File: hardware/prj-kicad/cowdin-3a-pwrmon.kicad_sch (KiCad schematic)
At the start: 2 parts, among them P1 CONN_9, P2 CONN_9

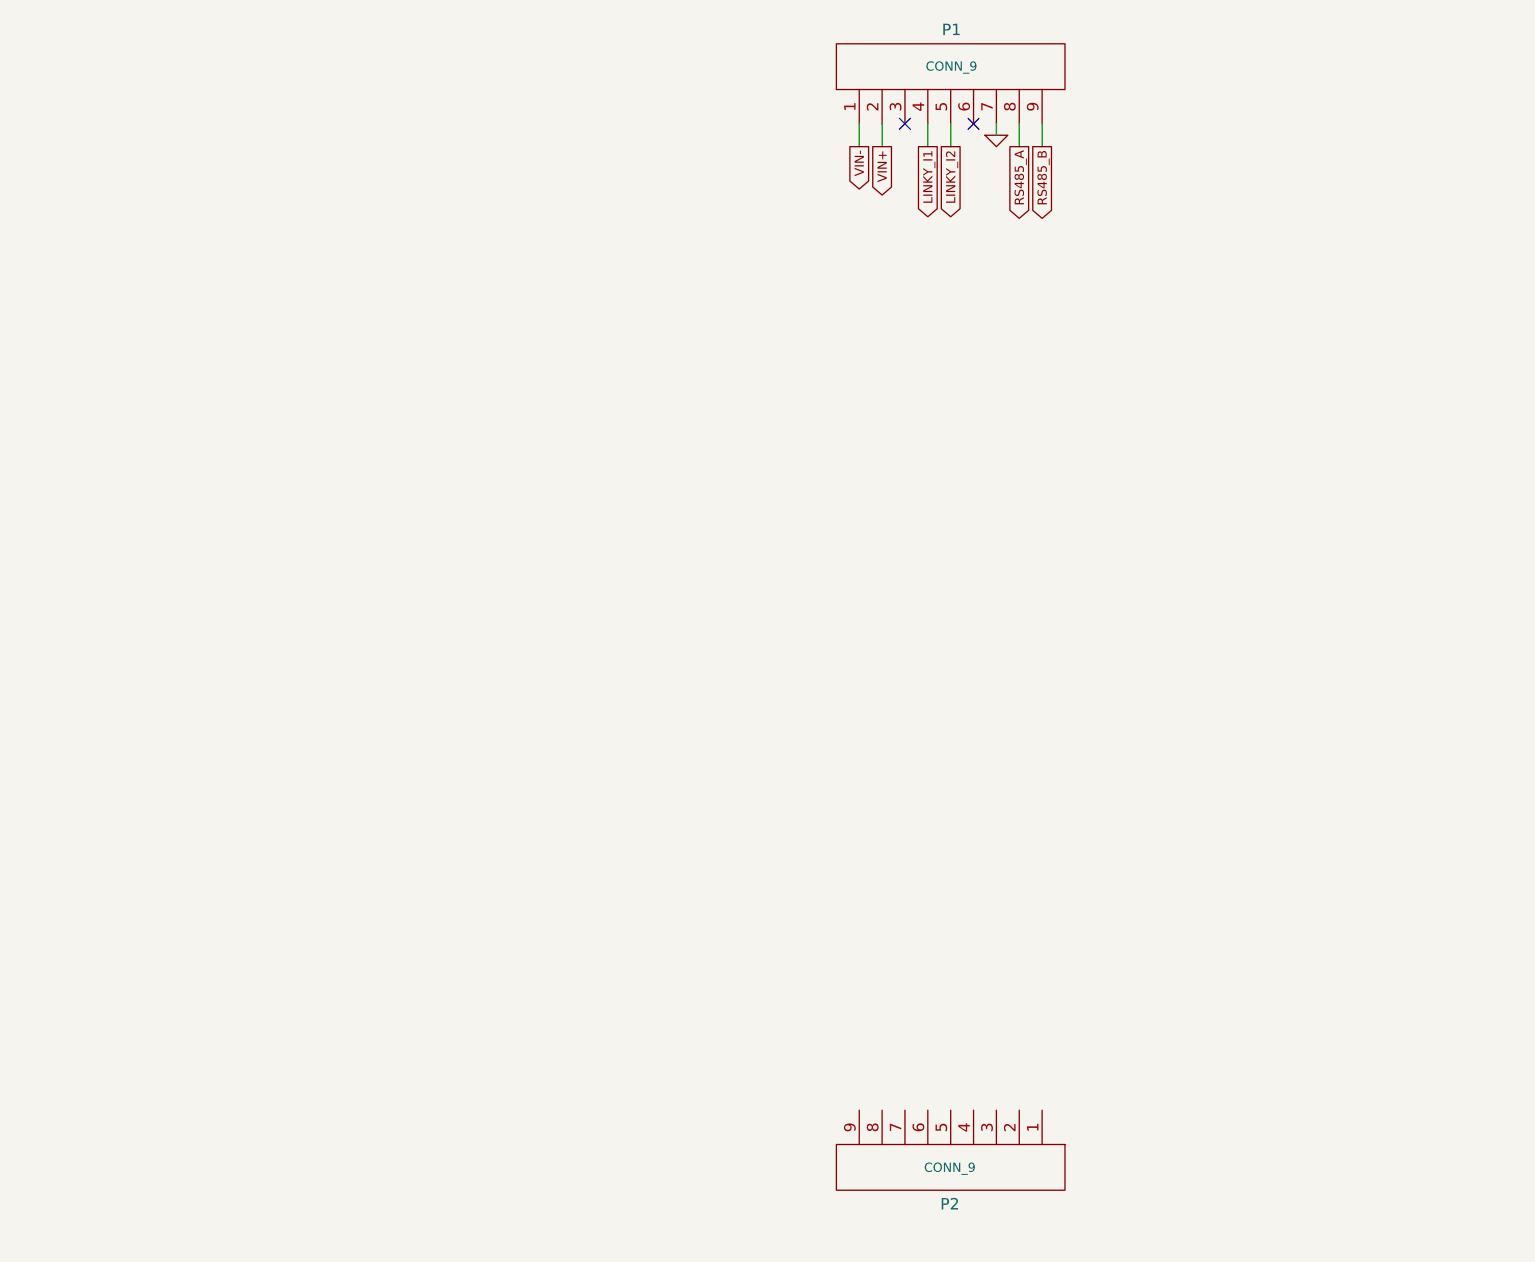
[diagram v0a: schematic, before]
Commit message: Hardware: Add communication interfaces (RS485 and Linky)
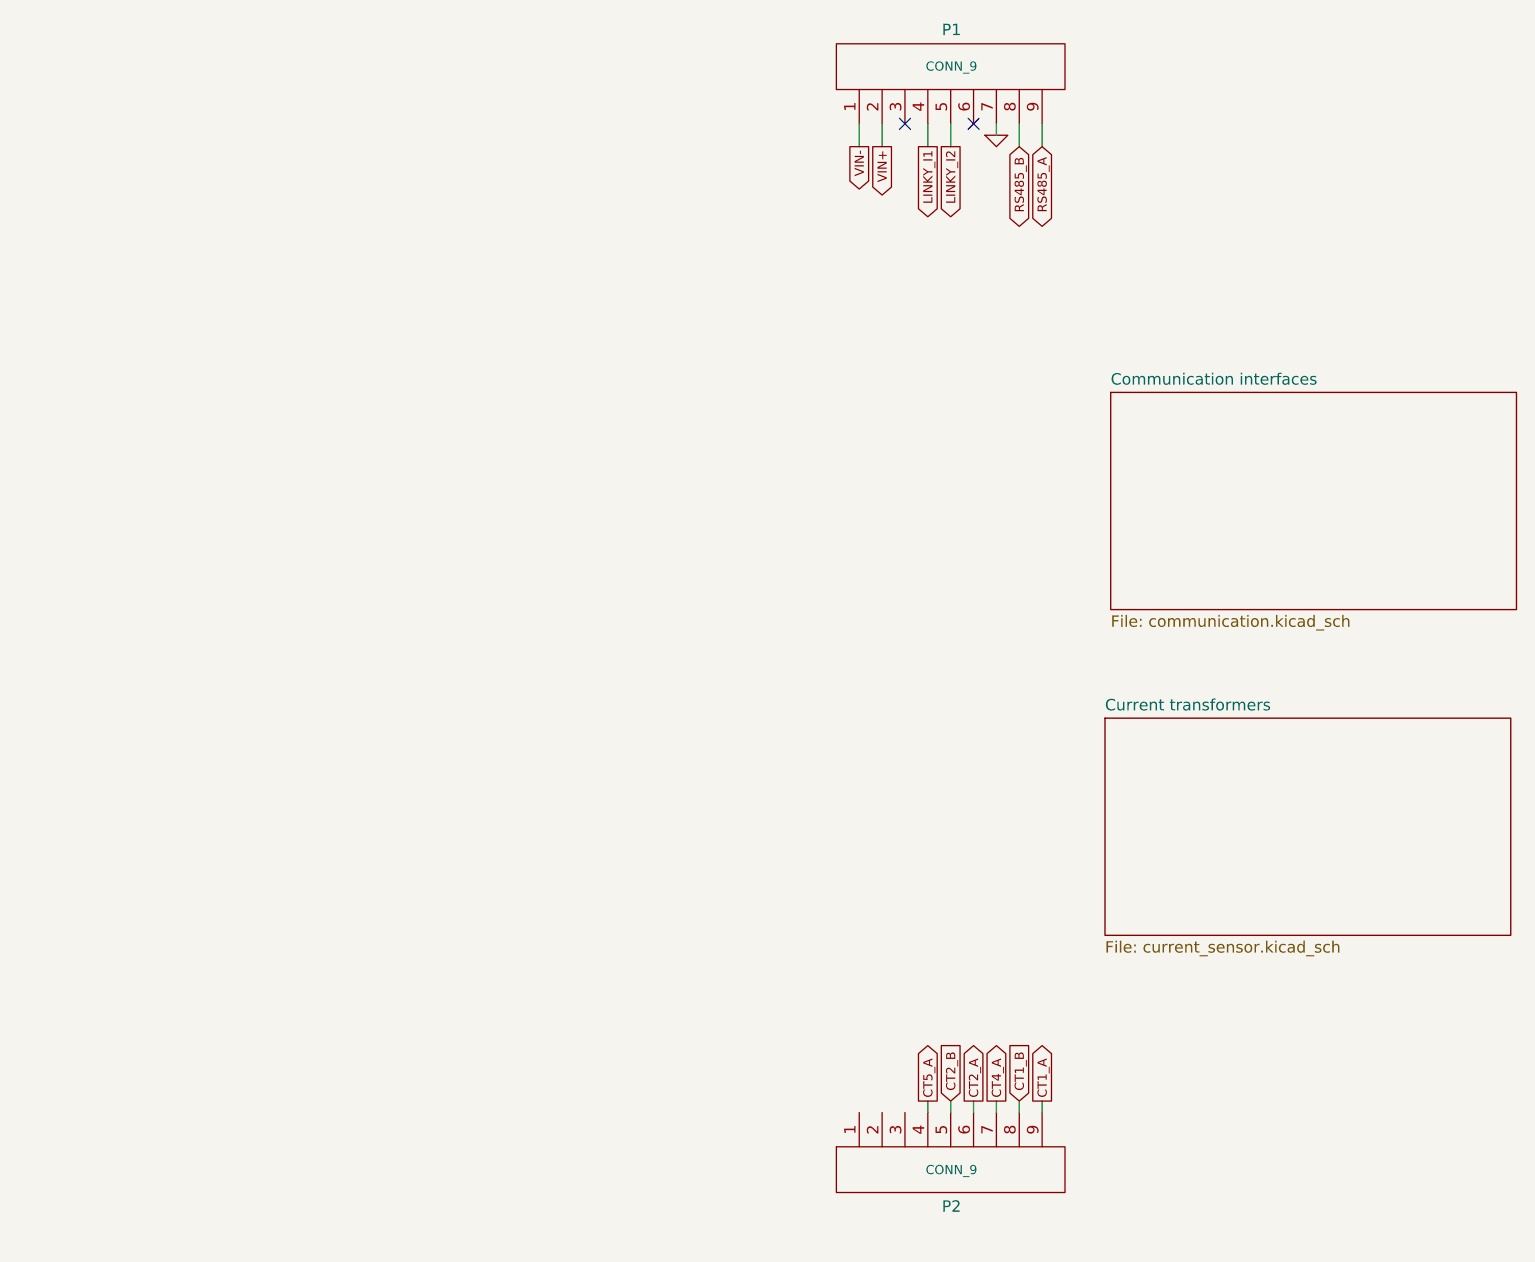
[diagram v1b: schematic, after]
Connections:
- net RS485_A: now also P1.9; no longer P1.8
- net RS485_B: now also P1.8; no longer P1.9
- net CT5_A: now reaches P2.4
- net CT2_B: now reaches P2.5
- net CT2_A: now reaches P2.6
- net CT4_A: now reaches P2.7
- net CT1_B: now reaches P2.8
- net CT1_A: now reaches P2.9
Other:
- added sheet Communication interfaces (communication.kicad_sch)
- added sheet Current transformers (current_sensor.kicad_sch)
- moved on the sheet: P2

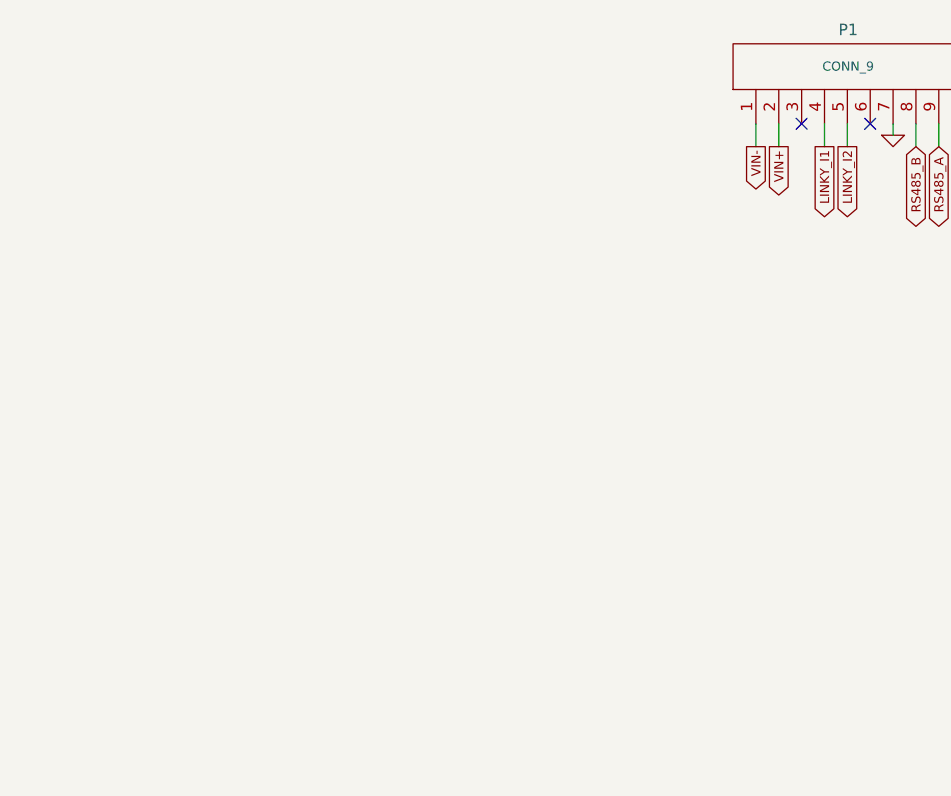
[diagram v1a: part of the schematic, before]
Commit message: Hardware: Add power supply
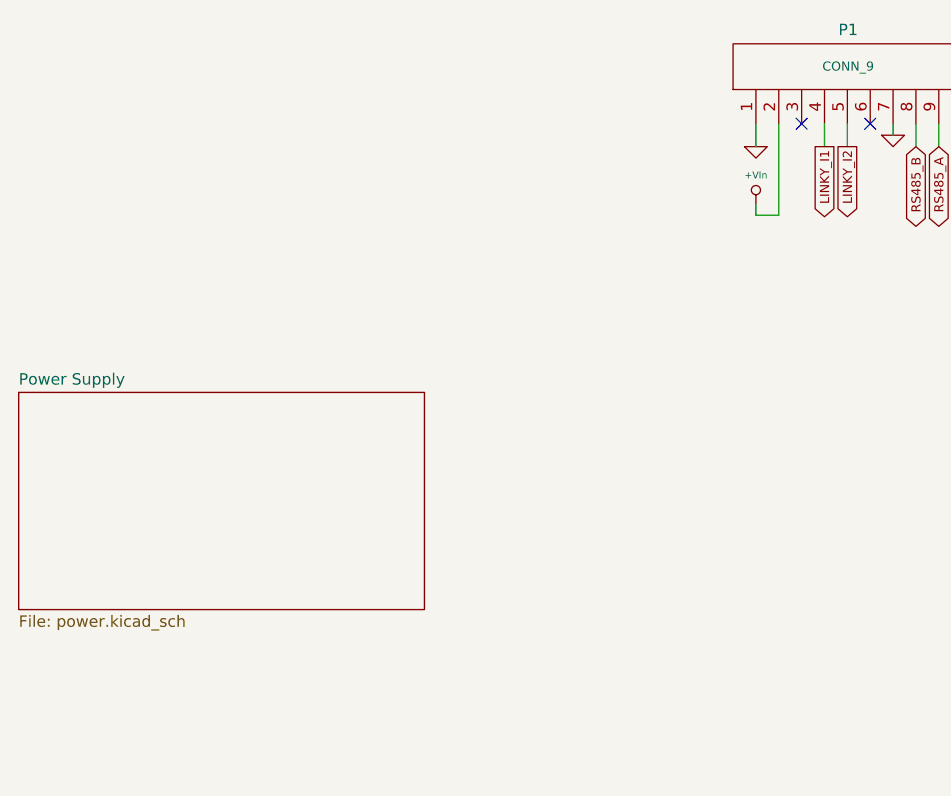
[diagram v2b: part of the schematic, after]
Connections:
- net VIN- is gone; now on net GND: P1.1
- net VIN+ renamed +VIn
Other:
- added sheet Power Supply (power.kicad_sch)

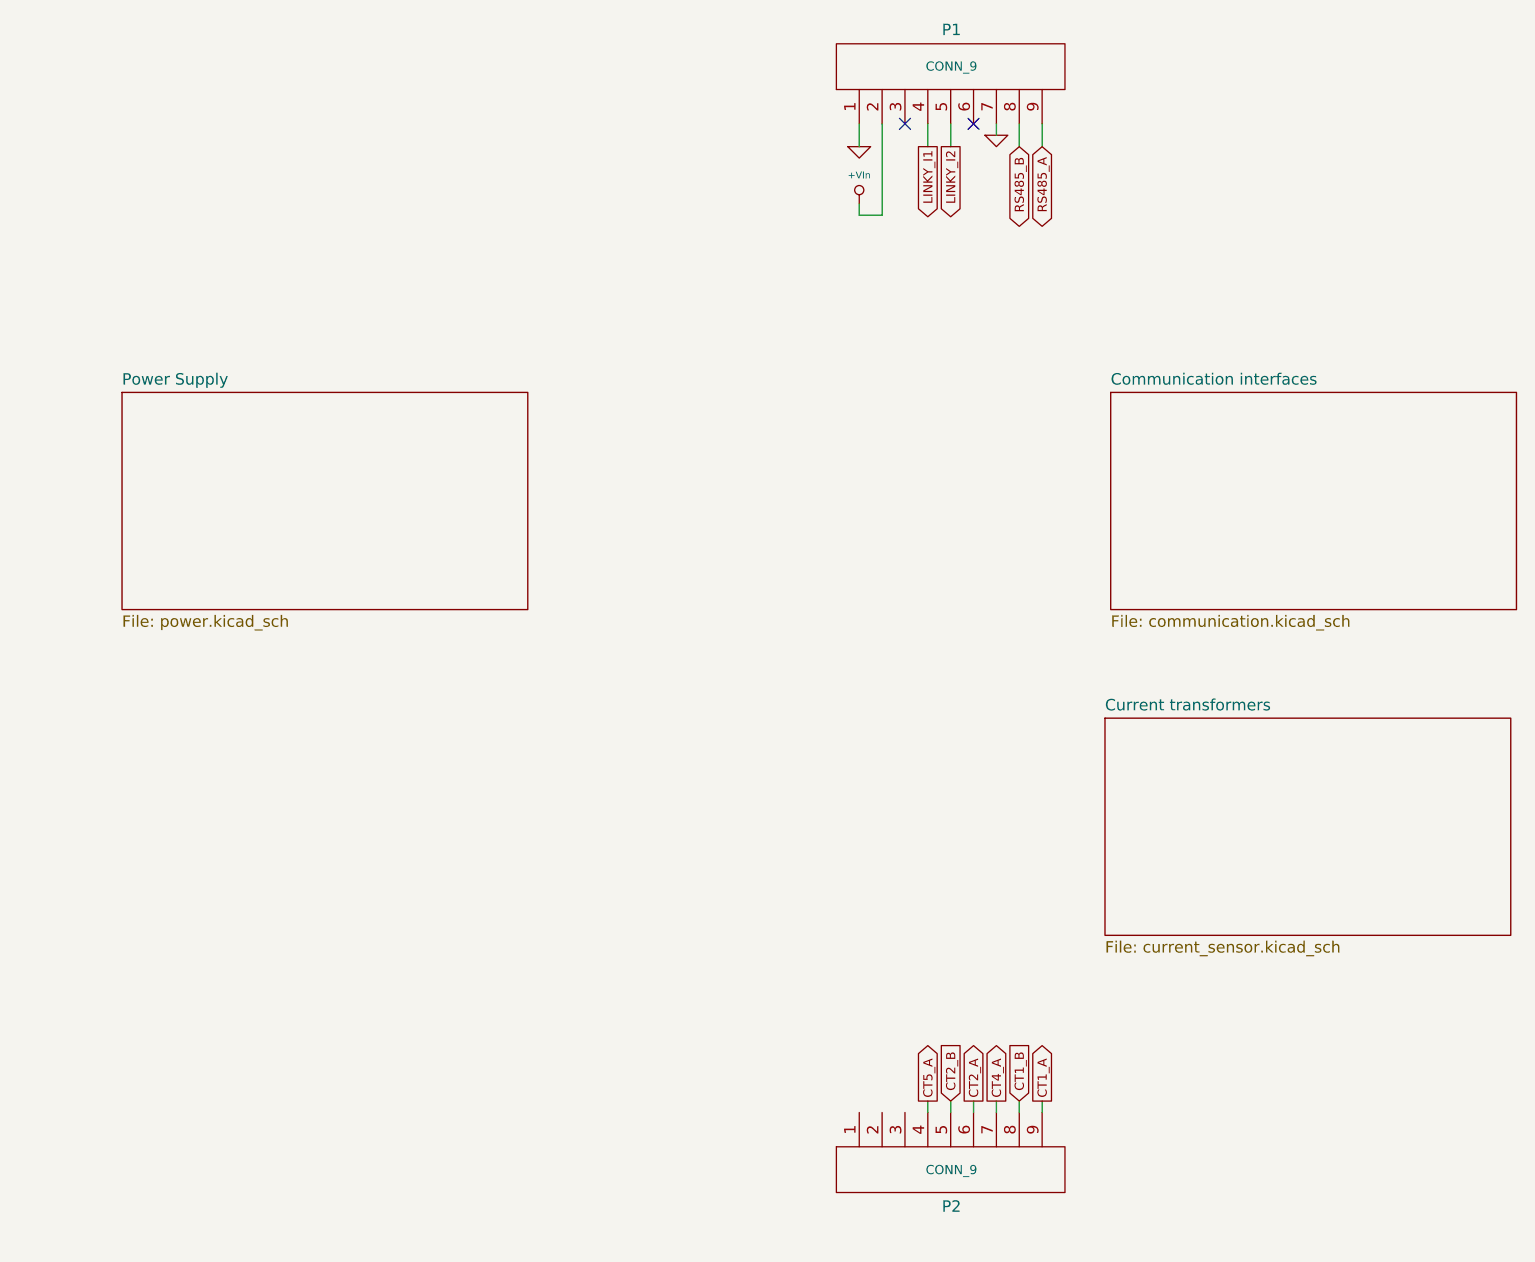
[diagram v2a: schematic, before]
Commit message: Hardware: Add processor (ATMSAMC21) and relay option
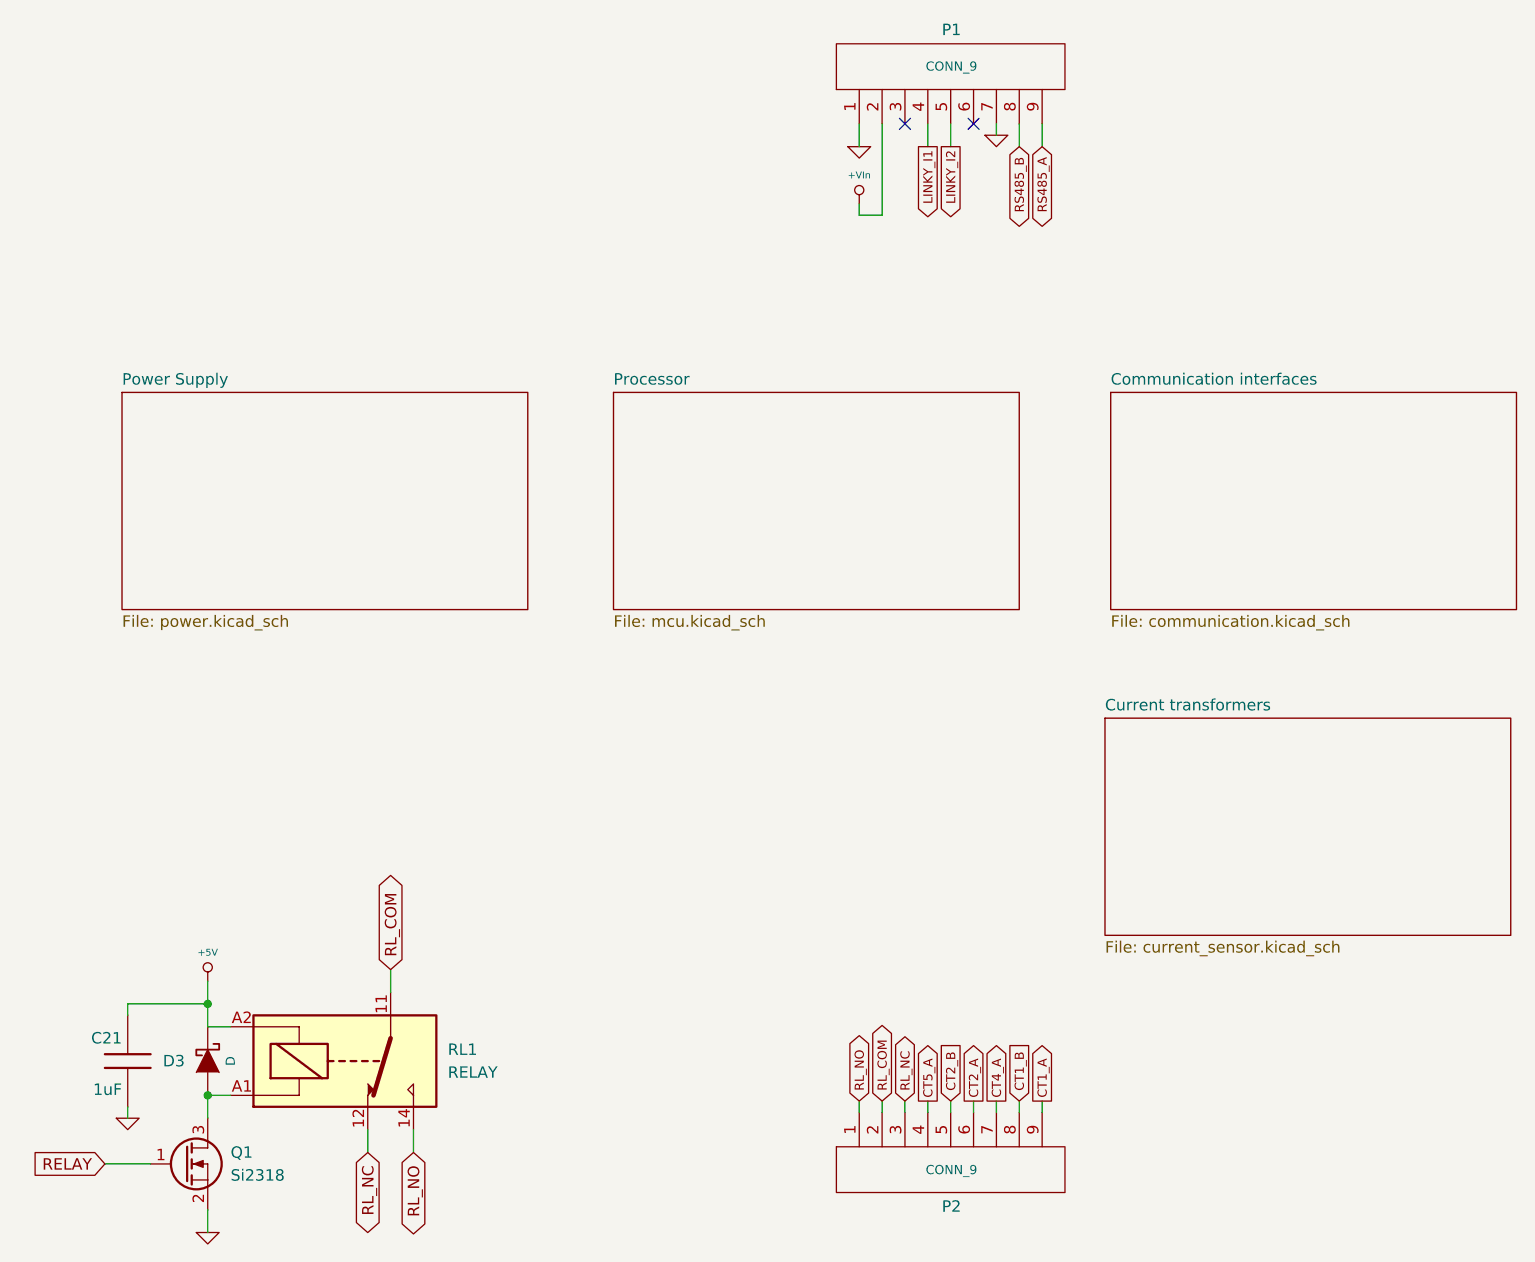
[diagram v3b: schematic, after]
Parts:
- added C21: 1uF, cowdin-3a-pwrmon:SMD0603, symbol cowdin-3a-pwrmon:C
- added D3: D, cowdin-3a-pwrmon:SOD-123, symbol cowdin-3a-pwrmon:D_Schottky
- added Q1: Si2318, cowdin-3a-pwrmon:SOT23-3, symbol cowdin-3a-pwrmon:Q_NMOS
- added RL1: RELAY, cowdin-3a-pwrmon:RL_3451, symbol cowdin-3a-pwrmon:RELAY
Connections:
- net GND: now also C21.2, Q1.2 (S)
- net RL_NO: now reaches P2.1
- net RL_NO: now also RL1.14
- net RL_COM: now reaches P2.2
- net RL_COM: now also RL1.11
- net RL_NC: now reaches P2.3
- net RL_NC: now also RL1.12
- new net: D3.1 (A), Q1.3 (D), RL1.A1
- new net +5V: C21.1, D3.2 (K), RL1.A2
- new net RELAY: Q1.1 (G)
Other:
- added sheet Processor (mcu.kicad_sch)
